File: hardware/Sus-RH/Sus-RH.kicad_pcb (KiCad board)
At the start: 2 copper layers, 36 parts, among them J1 MX150_02x06_Vertical, J2 53307-2471, J3 Conn_01x03, J5 Conn_01x06, U1 TLV9002QDRQ1, U2 LDO40LPURY

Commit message: finished layout
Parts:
- removed J3: Conn_01x03, Connector_PinSocket_2.54mm:PinSocket_1x03_P2.54mm_Vertical
- added D8: LED, LED_SMD:LED_0603_1608Metric_Pad1.05x0.95mm_HandSolder, F.Cu at (110.0, 49.5)
- added D9: LED, LED_SMD:LED_0603_1608Metric_Pad1.05x0.95mm_HandSolder, F.Cu at (110.0, 46.5)
- added G***: LOGO, UTSVT_Logos:UTSVT_Logo_Symbol, F.Cu at (87.4, 83.6)
- added G***: LHRs_LOGO, UTSVT_Logos:LHRs_LOGO, F.Cu at (108.0, 65.6)
- added J4: Conn_01x06, Connector_PinHeader_2.54mm:PinHeader_1x06_P2.54mm_Vertical, F.Cu at (107.8, 87.0)
- GND1, GNDA1, J1, ir_interrupt1, linpot_norm1, linpot_out1: moved to B.Cu
- J5: footprint Connector_Molex:Molex_Nano-Fit_105310-xx06_2x03_P2.50mm_Vertical -> Connector_Molex:Molex_Nano-Fit_105314-xx06_2x03_P2.50mm_Horizontal
- R11, R9: value 0 -> 1k
- R4, R5, R6, R7: value 1k -> 120
- moved R38 62.7 mm to (68.8, 52.3), turned to 90 degrees
- moved R7 62.4 mm to (89.0, 33.1), turned to 90 degrees
- moved R6 61.4 mm to (86.0, 33.1), turned to 90 degrees
- moved R10 56.5 mm to (96.8, 33.1), turned to 90 degrees
- moved R5 53.5 mm to (102.2, 33.0), turned to 90 degrees
- moved R8 53.3 mm to (93.8, 33.0), turned to 90 degrees
- moved R1 53.2 mm to (70.3, 52.3), turned to -90 degrees
- moved R2 52.4 mm to (72.8, 53.3), turned to 180 degrees
- moved C1 49.4 mm to (71.2, 49.5), turned to 180 degrees
- moved C2 46.7 mm to (77.6, 49.0), turned to 90 degrees
- moved F1 46.6 mm to (70.2, 30.6)
- moved U2 46.3 mm to (74.9, 50.5), turned to 180 degrees
- moved R11 42.9 mm to (106.7, 46.5)
- moved C3 41.3 mm to (87.8, 50.3), turned to 90 degrees
- moved RN1 36.9 mm to (75.3, 72.2), turned to 90 degrees
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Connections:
- C1 pad 1: +3.3V -> Net-(U2-Vout)
- J1 pad 2: /CAN_H -> /CAN_+
- J1 pad 3: /CAN_L -> /CAN_-
- J1 pad 8: /CAN_H -> /CAN_+
- J1 pad 9: /CAN_L -> /CAN_-
- J2 pad 12: unconnected-(J2-SPI2_NSS-Pad12) -> /SusConfig
- J2 pad 15: unconnected-(J2-ADC1_IN11-Pad15) -> /RHConfig
- J2 pad 16: unconnected-(J2-SPI2_MOSI-Pad16) -> /Debug2
- J2 pad 18: unconnected-(J2-SPI2_SCK-Pad18) -> /Debug1
- J2 pad 20: /CAN_L -> /CAN_-
- J2 pad 22: /CAN_H -> /CAN_+
- R10 pad 1: +3.3VMCU -> /SusConfig
- R10 pad 2: Net-(R10-Pad2) -> Net-(D7-A)
- R11 pad 1: Net-(R10-Pad2) -> /Debug1
- R11 pad 2: Net-(D7-A) -> Net-(D9-A)
- R8 pad 1: +3.3VMCU -> /RHConfig
- R8 pad 2: Net-(R8-Pad2) -> Net-(D6-A)
- R9 pad 1: Net-(R8-Pad2) -> /Debug2
- R9 pad 2: Net-(D6-A) -> Net-(D8-A)
- RN2 pad 1: /Gen_1 -> /Gen_4
- RN2 pad 2: /Gen_2 -> /Gen_3
- RN2 pad 3: /Gen_3 -> /Gen_2
- RN2 pad 4: /Gen_4 -> /Gen_1
- RN2 pad 5: GND -> +24V
- RN2 pad 6: /CAN_L -> /CAN_+
- RN2 pad 7: /CAN_H -> /CAN_-
- RN2 pad 8: +24V -> GND
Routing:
- net /IR_INTER: track 0.00 -> 84.7 mm, vias 0 -> 1
- net /linpot_out: track 0.00 -> 81.1 mm, vias 0 -> 5
- net +24V: track 0.00 -> 67.0 mm, vias 0 -> 4
- net /SCL: track 0.00 -> 64.6 mm
- net /SDA: track 0.00 -> 62.3 mm
- net /linpot_norm: track 0.00 -> 58.6 mm, vias 0 -> 4
- net /CAN_+: track 0.00 -> 45.4 mm
- net /CAN_-: track 0.00 -> 45.2 mm
- net GND: track 0.00 -> 43.8 mm, vias 0 -> 13
- net VDDA: track 0.00 -> 43.5 mm, vias 0 -> 2
- net GNDA: track 0.00 -> 42.2 mm, vias 0 -> 4
- net Net-(U2-Vout): track 0.00 -> 28.0 mm, vias 0 -> 1
- net /Debug1: track 0.00 -> 26.2 mm, vias 0 -> 4
- net /Debug2: track 0.00 -> 26.2 mm, vias 0 -> 2
- net +3.3V: track 0.00 -> 25.0 mm, vias 0 -> 13
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- added copper zone on F.Cu, net +3.3V
- added copper zone on B.Cu, net GND
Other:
- board outline added: 47.8 x 62 mm
- board text added: "+24v"
- board text added: "+3.3v"
- board text added: "Config"
- board text added: "Debug"
- board text added: "Karthik Kurapati"
- board text added: "MCU Power"
- board text added: "Power"
- board text added: "Status"

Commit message: fixed unity op-amp
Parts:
- G***: moved to B.Cu
- moved G*** 3.56 mm to (111.4, 66.7)

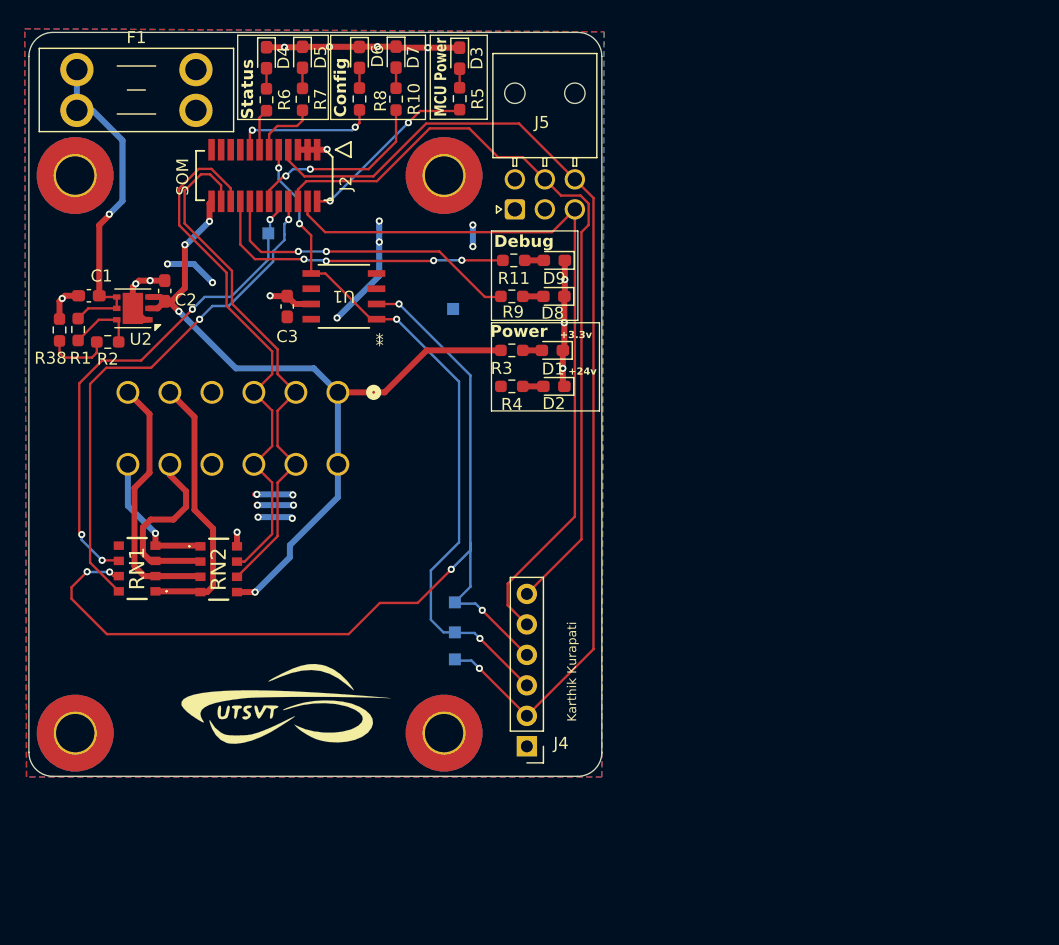
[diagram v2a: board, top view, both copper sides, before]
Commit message: added silkscreen, fixed rh-sus layout rh-sus done
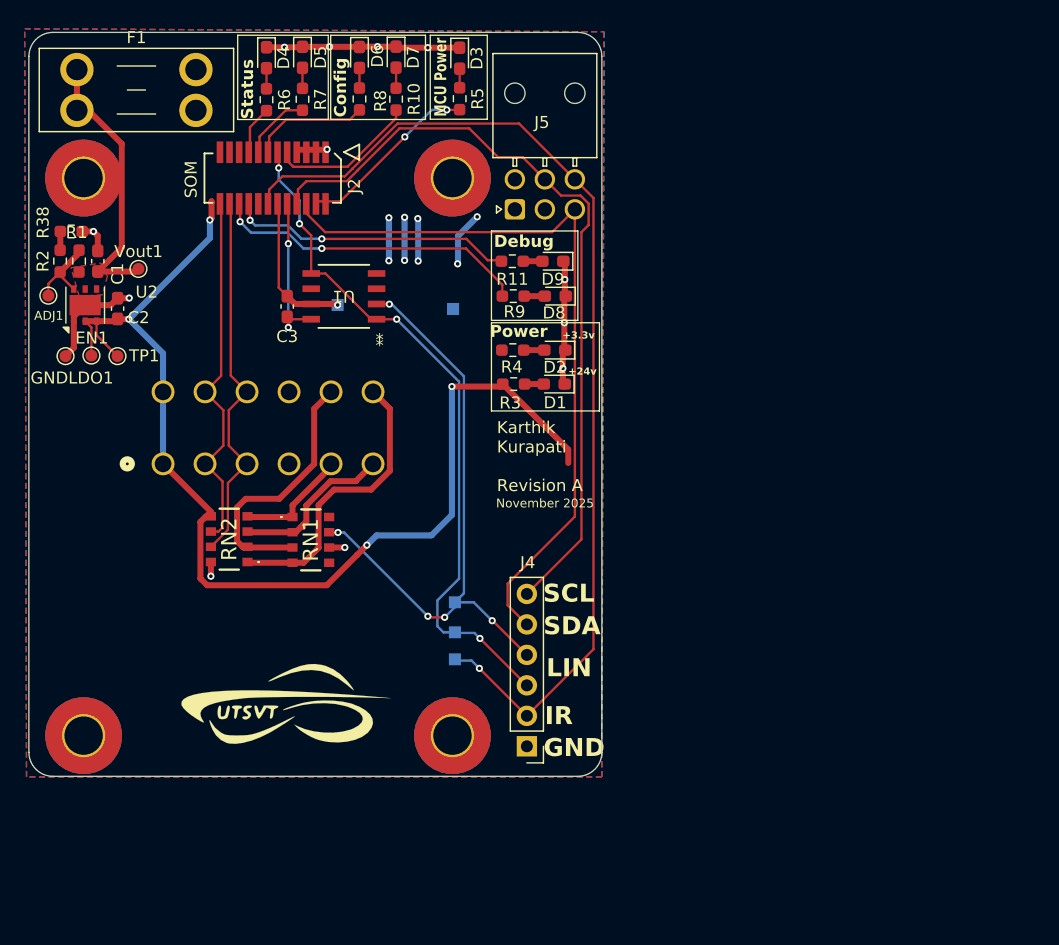
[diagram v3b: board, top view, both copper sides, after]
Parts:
- added ADJ1: TestPoint, TestPoint:TestPoint_Pad_D1.0mm, F.Cu at (67.9, 49.4)
- added EN1: TestPoint, TestPoint:TestPoint_Pad_D1.0mm, F.Cu at (71.5, 54.4)
- added G***: LOGO, UTSVT_Logos:roosters, B.Cu at (74.8, 73.9)
- added GNDLDO1: TestPoint, TestPoint:TestPoint_Pad_D1.0mm, F.Cu at (69.3, 54.5)
- added TP1: Vin, TestPoint:TestPoint_Pad_D1.0mm, F.Cu at (73.6, 54.5)
- added Vout1: TP1, TestPoint:TestPoint_Pad_D1.0mm, F.Cu at (75.4, 47.2)
- R3: value 1k -> 4.7k
- moved J1 15.7 mm to (77.4, 63.5), turned to 0 degrees
- moved RN1 14.7 mm to (89.7, 69.8), turned to -90 degrees
- moved GNDA1 8.31 mm to (92.0, 50.2)
- moved R38 8.27 mm to (69.8, 44.1), turned to 0 degrees
- moved R2 7.82 mm to (68.8, 46.6), turned to 90 degrees
- moved R1 5.70 mm to (70.4, 46.6), turned to 90 degrees
- moved C2 4.20 mm to (73.6, 50.5)
- moved U2 3.98 mm to (70.9, 50.2), turned to 90 degrees
- moved D2 3.02 mm to (110.1, 54.0)
- moved R4 3.02 mm to (106.6, 54.0)
- moved C1 2.97 mm to (72.0, 46.6), turned to 90 degrees
- moved D1 2.81 mm to (110.0, 56.8)
- moved R3 2.81 mm to (106.7, 56.8)
- moved RN2 2.65 mm to (82.9, 69.7), turned to 90 degrees
- moved J2 0.73 mm to (86.6, 39.6)
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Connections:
- C3 pad 1: +3.3V -> VDDA
- C3 pad 2: GND -> GNDA
- J2 pad 11: /LINPOT_STATUS -> /RHConfig
- J2 pad 12: /SusConfig -> /IR_INTER
- J2 pad 13: /RH_STATUS -> /LINPOT_STATUS
- J2 pad 15: /RHConfig -> /RH_STATUS
- J2 pad 16: /Debug2 -> /Debug1
- J2 pad 18: /Debug1 -> /Debug2
- J2 pad 7: /IR_INTER -> /SusConfig
- RN1 pad 6: GNDA -> GND
- RN1 pad 8: VDDA -> +3.3V
- U1 pad 7: GND -> GNDA
- U1 pad 8: +3.3V -> VDDA
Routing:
- net /linpot_out: track 81.1 -> 51.1 mm
- net VDDA: track 43.5 -> 13.5 mm
- net GNDA: track 42.2 -> 12.7 mm, vias 4 -> 1
- net +24V: track 67.0 -> 95.8 mm
- net +3.3V: track 25.0 -> 0.00 mm, vias 13 -> 0
- net (no net): track 0.00 -> 15.5 mm, vias 0 -> 8
- net /CAN_+: track 45.4 -> 31.4 mm
- net /CAN_-: track 45.2 -> 31.9 mm
- net /Gen_1: track 22.7 -> 9.53 mm
- net /Gen_4: track 11.5 -> 24.3 mm, vias 1 -> 0
- net /Gen_2: track 21.6 -> 13.7 mm
- net /Gen_3: track 15.7 -> 22.2 mm
- net Net-(U2-Vout): track 28.0 -> 23.3 mm, vias 1 -> 0
- net Net-(R2-Pad2): track 5.45 -> 1.56 mm
- net /SusConfig: track 15.8 -> 12.5 mm, vias 2 -> 0
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- added copper zone on F.Cu, net Net-(U2-Vout)
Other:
- board text added: "GND"
- board text added: "IR"
- board text added: "Karthik Kurapati Revision A"
- board text added: "LIN"
- board text added: "November 2025"
- board text added: "SCL"
- board text added: "SDA"
- board text removed: "Karthik Kurapati"

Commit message: sus rh changes + gerbers
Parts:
- moved J2 0.77 mm to (85.8, 39.6)
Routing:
- net (no net): track 15.5 -> 0.00 mm, vias 8 -> 0
- net +24V: track 95.8 -> 87.1 mm
- net +3.3V: track 0.00 -> 4.53 mm, vias 0 -> 2
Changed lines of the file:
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@@
 	(footprint "UTSVT_Connectors:PeripheralSOM"
 		(layer "F.Cu")
-		(at 86.57 39.64)
+		(at 85.8 39.64)
 		(property "Reference" "J2"
 			(at 6.8 0.67 90)
@@
 	)
 	(segment
-		(start 96.25 46.57)
-		(end 96.25 46.53)
-		(width 0.5)
-		(layer "F.Cu")
-		(net 0)
-	)
-	(segment
-		(start 102.01 46.76)
-		(end 101.98 46.79)
-		(width 0.5)
-		(layer "F.Cu")
-		(net 0)
-	)
-	(segment
-		(start 98.69 46.62)
-		(end 98.69 46.55)
-		(width 0.5)
-		(layer "F.Cu")
-		(net 0)
-	)
-	(via
-		(at 98.66 43.02)
-		(size 0.6)
-		(drill 0.3)
-		(layers "F.Cu" "B.Cu")
-		(net 0)
-	)
-	(via
-		(at 96.25 46.53)
-		(size 0.6)
-		(drill 0.3)
-		(layers "F.Cu" "B.Cu")
-		(net 0)
-	)
-	(via
-		(at 98.69 46.55)
-		(size 0.6)
-		(drill 0.3)
-		(layers "F.Cu" "B.Cu")
-		(net 0)
-	)
-	(via
-		(at 97.56 42.91)
-		(size 0.6)
-		(drill 0.3)
-		(layers "F.Cu" "B.Cu")
-		(net 0)
-	)
-	(via
-		(at 97.56 46.5)
-		(size 0.6)
-		(drill 0.3)
-		(layers "F.Cu" "B.Cu")
-		(net 0)
-	)
-	(via
-		(at 103.61 42.87)
-		(size 0.6)
-		(drill 0.3)
-		(layers "F.Cu" "B.Cu")
-		(net 0)
-	)
-	(via
-		(at 96.25 42.95)
-		(size 0.6)
-		(drill 0.3)
-		(layers "F.Cu" "B.Cu")
-		(net 0)
-	)
-	(via
-		(at 101.98 46.79)
-		(size 0.6)
-		(drill 0.3)
-		(layers "F.Cu" "B.Cu")
-		(net 0)
-	)
-	(segment
-		(start 102.01 44.47)
-		(end 103.61 42.87)
-		(width 0.5)
-		(layer "B.Cu")
-		(net 0)
-	)
-	(segment
-		(start 97.56 46.5)
-		(end 97.56 42.91)
-		(width 0.5)
-		(layer "B.Cu")
-		(net 0)
-	)
-	(segment
-		(start 98.69 46.55)
-		(end 98.69 43.05)
-		(width 0.5)
-		(layer "B.Cu")
-		(net 0)
-	)
-	(segment
-		(start 101.98 46.79)
-		(end 102.01 46.76)
-		(width 0.5)
-		(layer "B.Cu")
-		(net 0)
-	)
-	(segment
-		(start 102.01 46.76)
-		(end 102.01 44.47)
-		(width 0.5)
-		(layer "B.Cu")
-		(net 0)
-	)
-	(segment
-		(start 96.25 46.53)
-		(end 96.25 42.95)
-		(width 0.5)
-		(layer "B.Cu")
-		(net 0)
-	)
-	(segment
-		(start 98.69 43.05)
-		(end 98.66 43.02)
-		(width 0.5)
-		(layer "B.Cu")
-		(net 0)
-	)
-	(segment
 		(start 96.9375 28.775)
 		(end 96.85 28.6875)
@@
 		(net 1)
 	)
+	(via
+		(at 104.1 43)
+		(size 0.6)
+		(drill 0.3)
+		(layers "F.Cu" "B.Cu")
+		(free yes)
+		(net 2)
+	)
+	(via
+		(at 102.1 46.7)
+		(size 0.6)
+		(drill 0.3)
+		(layers "F.Cu" "B.Cu")
+		(free yes)
+		(net 2)
+	)
+	(segment
+		(start 102.1 45)
+		(end 104.1 43)
+		(width 0.5)
+		(layer "B.Cu")
+		(net 2)
+	)
+	(segment
+		(start 102.1 46.7)
+		(end 102.1 45)
+		(width 0.5)
+		(layer "B.Cu")
+		(net 2)
+	)
 	(segment
 		(start 81.47 43)
@@
 	)
 	(segment
-		(start 70.94 51.57)
-		(end 73.45 51.57)
-		(width 0.5)
-		(layer "F.Cu")
-		(net 3)
-	)
-	(segment
 		(start 91.077005 73.574995)
 		(end 81.102925 73.574995)
@@
 	)
 	(segment
-		(start 105.74125 56.81)
-		(end 111.199 62.26775)
+		(start 71.07 51.7)
+		(end 73.32 51.7)
 		(width 0.5)
 		(layer "F.Cu")
@@
 	)
 	(segment
-		(start 111.199 62.26775)
-		(end 111.199 63.39)
-		(width 0.5)
-		(layer "F.Cu")
-		(net 3)
-	)
-	(segment
 		(start 93.609265 71.040735)
 		(end 93.609265 71.042735)
@@
 	)
 	(segment
-		(start 73.45 51.57)
-		(end 73.64 51.38)
-		(width 0.5)
+		(start 71.89 51.57)
+		(end 71.89 52.74)
+		(width 0.2)
 		(layer "F.Cu")
 		(net 3)
 	)
 	(segment
-		(start 71.89 51.57)
-		(end 71.89 52.74)
-		(width 0.2)
+		(start 73.32 51.7)
+		(end 73.64 51.38)
+		(width 0.5)
 		(layer "F.Cu")
 		(net 3)
@@
 		(net 3)
 	)
+	(segment
+		(start 70.94 51.57)
+		(end 71.07 51.7)
+		(width 0.5)
+		(layer "F.Cu")
+		(net 3)
+	)
 	(via
 		(at 101.5 57.016765)
@@
 	(segment
 		(start 111.75 42.25)
-		(end 109.85 44.15)
+		(end 112 42.5)
 		(width 0.2)
 		(layer "F.Cu")
@@
 	)
 	(segment
-		(start 109.85 44.15)
-		(end 90.94 44.15)
+		(start 112 67.6)
+		(end 106.15 73.45)
 		(width 0.2)
 		(layer "F.Cu")
@@
 	(segment
 		(start 111.75 42.25)
-		(end 111.75 67.85)
+		(end 109.85 44.15)
+		(width 0.2)
+		(layer "F.Cu")
+		(net 18)
+	)
+	(segment
+		(start 109.85 44.15)
+		(end 90.94 44.15)
 		(width 0.2)
 		(layer "F.Cu")
@@
 	)
 	(segment
-		(start 111.75 67.85)
-		(end 106.15 73.45)
+		(start 106.15 73.45)
+		(end 106.15 75.24)
 		(width 0.2)
 		(layer "F.Cu")
@@
 	)
 	(segment
-		(start 106.15 73.45)
-		(end 106.15 75.24)
+		(start 112 42.5)
+		(end 112 67.6)
 		(width 0.2)
 		(layer "F.Cu")
@@
 	)
 	(segment
-		(start 88.28 38.7)
-		(end 92.81 38.7)
+		(start 87.87 38.47)
+		(end 88.1 38.7)
 		(width 0.2)
 		(layer "F.Cu")
@@
 	)
 	(segment
-		(start 87.87 38.29)
-		(end 88.28 38.7)
+		(start 87.87 37.28)
+		(end 87.87 38.47)
 		(width 0.2)
 		(layer "F.Cu")
@@
 	)
 	(segment
-		(start 87.87 37.28)
-		(end 87.87 38.29)
+		(start 92.81 38.7)
+		(end 92.81 38.69)
 		(width 0.2)
 		(layer "F.Cu")
@@
 	)
 	(segment
-		(start 92.81 38.69)
-		(end 96.85 34.65)
+		(start 88.1 38.7)
+		(end 92.81 38.7)
 		(width 0.2)
 		(layer "F.Cu")
@@
 	)
 	(segment
-		(start 92.81 38.7)
-		(end 92.81 38.69)
+		(start 92.81 38.69)
+		(end 96.85 34.65)
 		(width 0.2)
 		(layer "F.Cu")
@@
 	)
 	(segment
-		(start 112.3 69.75)
+		(start 112.901 69.149)
 		(end 107.75 74.3)
 		(width 0.2)
@@
 	)
 	(segment
-		(start 112.901 41.77324)
-		(end 112.901 43.549)
+		(start 110.599 41.099)
+		(end 112.22676 41.099)
 		(width 0.2)
 		(layer "F.Cu")
@@
 	)
 	(segment
-		(start 110.599 41.099)
-		(end 112.22676 41.099)
-		(width 0.2)
-		(layer "F.Cu")
-		(net 40)
-	)
-	(segment
-		(start 109.25 39.75)
-		(end 110.599 41.099)
-		(width 0.2)
-		(layer "F.Cu")
-		(net 40)
-	)
-	(segment
 		(start 89.373 39.9)
 		(end 92.7442 39.9)
@@
 	)
 	(segment
-		(start 112.901 43.549)
-		(end 112.3 44.15)
+		(start 92.7442 39.9)
+		(end 93.612 39.0322)
 		(width 0.2)
 		(layer "F.Cu")
@@
 	)
 	(segment
-		(start 92.7442 39.9)
-		(end 93.612 39.0322)
+		(start 112.901 41.77324)
+		(end 112.901 69.149)
 		(width 0.2)
 		(layer "F.Cu")
@@
 	)
 	(segment
-		(start 112.3 44.15)
-		(end 112.3 69.75)
+		(start 109.25 39.75)
+		(end 110.599 41.099)
 		(width 0.2)
 		(layer "F.Cu")
